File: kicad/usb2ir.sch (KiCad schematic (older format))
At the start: 41 parts, among them J1 USB_A, J2 Conn_01x04_Male, Q1 S8050, Q2 S8050, SW1 SW_Push, U1 YK003, U2 CH340G, U3 LM1117-3.3, U4 STM32F103RBTx, Y1 12M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

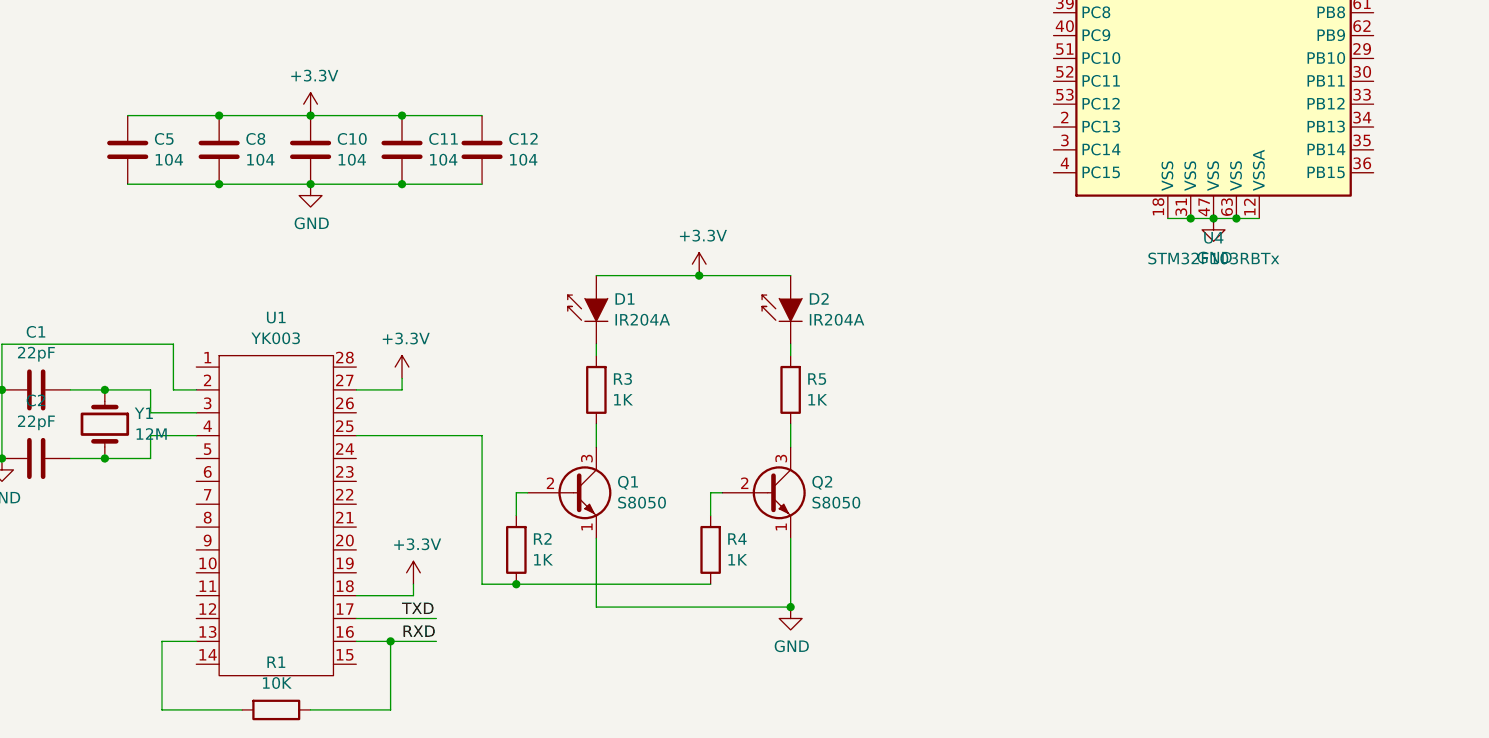
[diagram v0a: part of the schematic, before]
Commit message: 硬件添加红外复制功能
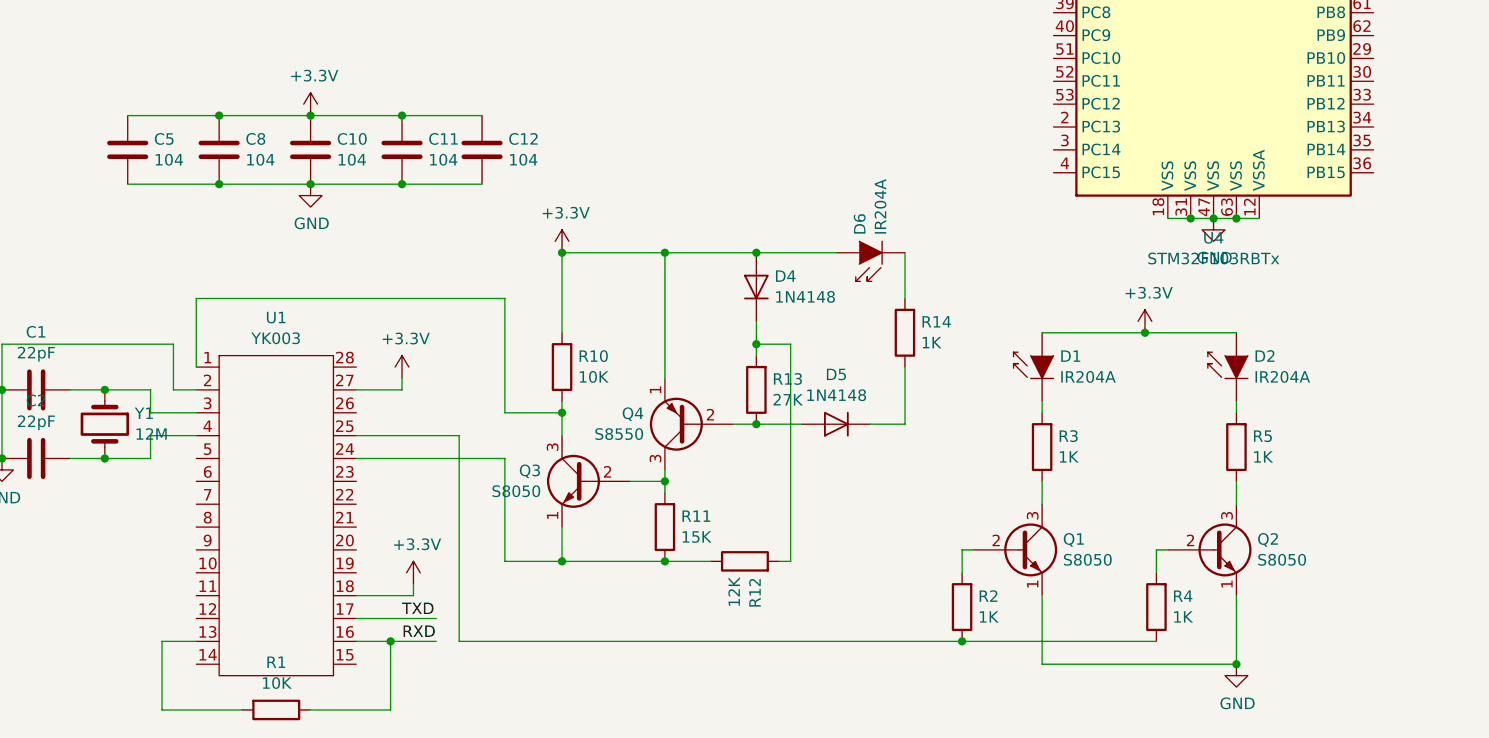
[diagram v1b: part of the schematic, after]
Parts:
- added D4, D5: 1N4148, Diode_SMD:D_0603_1608Metric_Castellated, symbol Diode:1N4148
- added D6: IR204A, LED_THT:LED_D3.0mm_IRBlack, symbol LED:IR204A
- added Q3: S8050, Package_TO_SOT_SMD:SOT-23, symbol Transistor_BJT:S8050
- added Q4: S8550, Package_TO_SOT_SMD:SOT-23, symbol Transistor_BJT:S8550
- added R10: 10K, Resistor_SMD:R_0603_1608Metric_Pad1.05x0.95mm_HandSolder, symbol Device:R
- added R11: 15K, Resistor_SMD:R_0603_1608Metric_Pad1.05x0.95mm_HandSolder, symbol Device:R
- added R12: 12K, Resistor_SMD:R_0603_1608Metric_Pad1.05x0.95mm_HandSolder, symbol Device:R
- added R13: 27K, Resistor_SMD:R_0603_1608Metric_Pad1.05x0.95mm_HandSolder, symbol Device:R
- added R14: 1K, Resistor_SMD:R_0603_1608Metric_Pad1.05x0.95mm_HandSolder, symbol Device:R
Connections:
- wire segments 132 -> 162
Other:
- moved on the sheet: D1, D2, Q1, Q2, R2, R3, R4, R5

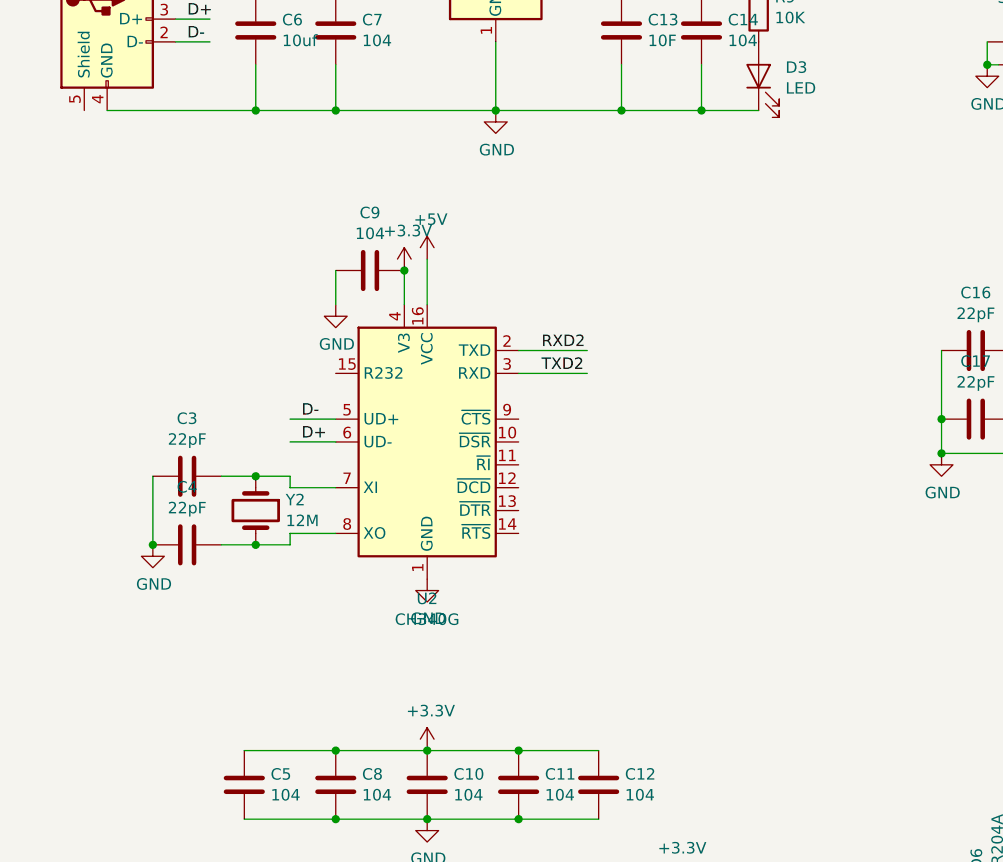
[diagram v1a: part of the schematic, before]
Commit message: 经过长时间的运行发现CH340G偶尔会出现数据丢失情况故现改用cp2104增加稳定性
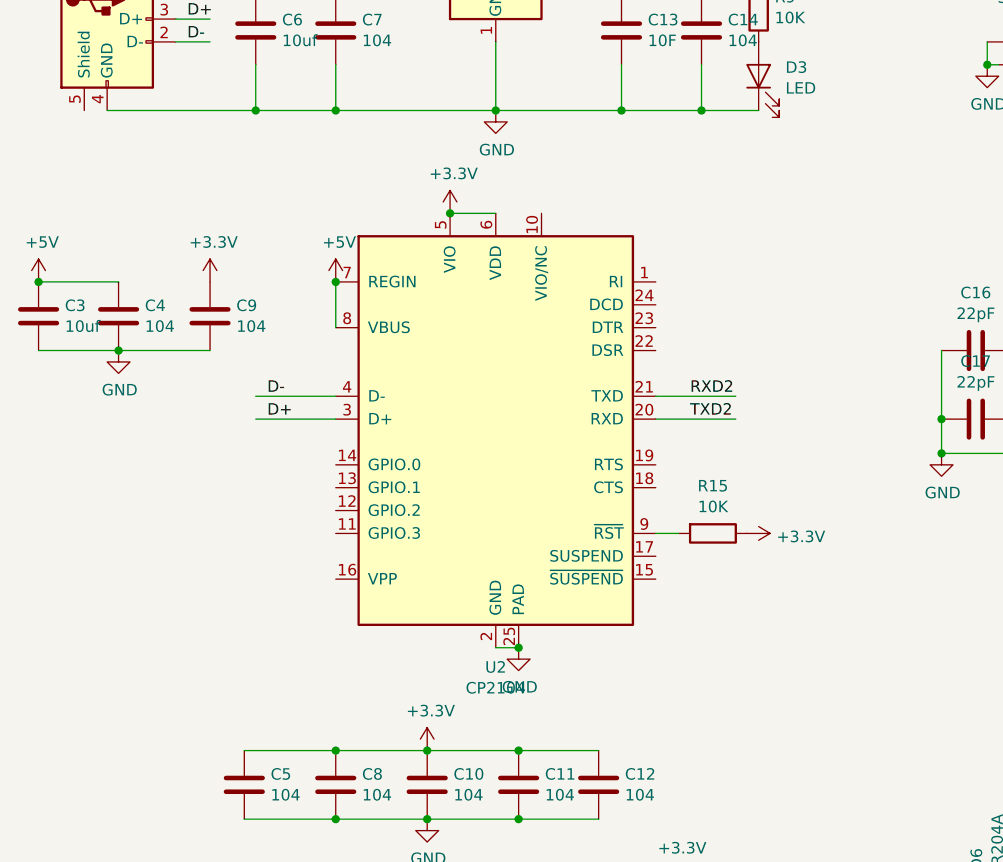
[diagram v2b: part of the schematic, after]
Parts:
- removed U2: CH340G, Package_SO:SOIC-16_3.9x9.9mm_P1.27mm, symbol Interface_USB:CH340G
- removed Y2: 12M, Crystal:Crystal_SMD_5032-2Pin_5.0x3.2mm, symbol Device:Crystal
- added R15: 10K, Resistor_SMD:R_0603_1608Metric_Pad1.05x0.95mm_HandSolder, symbol Device:R
- added U2: CP2104, Package_DFN_QFN:QFN-24-1EP_4x4mm_P0.5mm_EP2.6x2.6mm, symbol Interface_USB:CP2104
- C3: value 22pF -> 10uf
- C4: value 22pF -> 104
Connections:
- wire segments 162 -> 157
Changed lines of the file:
@@
-	1    0    0    -1
-$EndComp
-$Comp
-L Interface_USB:CH340G U2
-U 1 1 6507D2A5
-P 2550 3200
-F 0 "U2" H 2550 2514 50  0000 C CNN
-F 1 "CH340G" H 2550 2423 50  0000 C CNN
-F 2 "Package_SO:SOIC-16_3.9x9.9mm_P1.27mm" H 2600 2650 50  0001 L CNN
-F 3 "http://www.datasheet5.com/pdf-local-2195953" H 2200 4000 50  0001 C CNN
-	1    2550 3200
 	1    0    0    -1
 $EndComp
@@
 Text Label 1500 1450 0    50   ~ 0
 D-
-Text Label 2000 3200 0    50   ~ 0
-D+
-Text Label 2000 3100 0    50   ~ 0
-D-
-Wire Wire Line
-	2150 3100 1950 3100
-Wire Wire Line
-	2150 3200 1950 3200
-$Comp
-L Device:Crystal Y2
-U 1 1 6507DC27
-P 1800 3500
-F 0 "Y2" V 1754 3631 50  0000 L CNN
-F 1 "12M" V 1845 3631 50  0000 L CNN
-F 2 "Crystal:Crystal_SMD_5032-2Pin_5.0x3.2mm" H 1800 3500 50  0001 C CNN
-F 3 "~" H 1800 3500 50  0001 C CNN
-	1    1800 3500
-	0    1    1    0
-$EndComp
-Wire Wire Line
-	1800 3350 1950 3350
-Wire Wire Line
-	1950 3350 1950 3400
-Wire Wire Line
-	1950 3400 2150 3400
-Wire Wire Line
-	1800 3650 1950 3650
-Wire Wire Line
-	1950 3650 1950 3600
-Wire Wire Line
-	1950 3600 2150 3600
-$Comp
-L Device:C C4
-U 1 1 6507E9BB
-P 1500 3650
-F 0 "C4" V 1248 3650 50  0000 C CNN
-F 1 "22pF" V 1339 3650 50  0000 C CNN
-F 2 "Capacitor_SMD:C_0603_1608Metric" H 1538 3500 50  0001 C CNN
-F 3 "~" H 1500 3650 50  0001 C CNN
-	1    1500 3650
-	0    1    1    0
-$EndComp
-$Comp
-L Device:C C3
-U 1 1 6507F0B7
-P 1500 3350
-F 0 "C3" V 1248 3350 50  0000 C CNN
-F 1 "22pF" V 1339 3350 50  0000 C CNN
-F 2 "Capacitor_SMD:C_0603_1608Metric" H 1538 3200 50  0001 C CNN
-F 3 "~" H 1500 3350 50  0001 C CNN
-	1    1500 3350
-	0    1    1    0
-$EndComp
-Wire Wire Line
-	1650 3350 1800 3350
-Connection ~ 1800 3350
-Wire Wire Line
-	1800 3650 1650 3650
-Connection ~ 1800 3650
-Wire Wire Line
-	1350 3650 1350 3350
-$Comp
-L power:GND #PWR02
-U 1 1 6507FC4A
-P 1350 3650
-F 0 "#PWR02" H 1350 3400 50  0001 C CNN
-F 1 "GND" H 1355 3477 50  0000 C CNN
-F 2 "" H 1350 3650 50  0001 C CNN
-F 3 "" H 1350 3650 50  0001 C CNN
-	1    1350 3650
-	1    0    0    -1
-$EndComp
-Connection ~ 1350 3650
-Wire Wire Line
-	2950 2800 3250 2800
-Wire Wire Line
-	2950 2900 3250 2900
-Text Label 3050 2800 0    50   ~ 0
-RXD2
-Text Label 3050 2900 0    50   ~ 0
-TXD2
-Wire Wire Line
-	2550 2400 2550 2600
-$Comp
-L power:GND #PWR07
-U 1 1 6508135F
-P 2550 3800
-F 0 "#PWR07" H 2550 3550 50  0001 C CNN
-F 1 "GND" H 2555 3627 50  0000 C CNN
-F 2 "" H 2550 3800 50  0001 C CNN
-F 3 "" H 2550 3800 50  0001 C CNN
-	1    2550 3800
-	1    0    0    -1
-$EndComp
-$Comp
-L power:GND #PWR04
-U 1 1 6508139E
-P 2150 2600
-F 0 "#PWR04" H 2150 2350 50  0001 C CNN
-F 1 "GND" H 2155 2427 50  0000 C CNN
-F 2 "" H 2150 2600 50  0001 C CNN
-F 3 "" H 2150 2600 50  0001 C CNN
-	1    2150 2600
-	1    0    0    -1
-$EndComp
-$Comp
-L Device:C C9
-U 1 1 650813F5
-P 2300 2450
-F 0 "C9" V 2048 2450 50  0000 C CNN
-F 1 "104" V 2139 2450 50  0000 C CNN
-F 2 "Capacitor_SMD:C_0603_1608Metric" H 2338 2300 50  0001 C CNN
-F 3 "~" H 2300 2450 50  0001 C CNN
-	1    2300 2450
-	0    1    1    0
-$EndComp
-Wire Wire Line
-	2150 2600 2150 2450
-Wire Wire Line
-	2450 2600 2450 2450
-$Comp
-L power:+5V #PWR06
-U 1 1 65081DD3
-P 2550 2400
-F 0 "#PWR06" H 2550 2250 50  0001 C CNN
-F 1 "+5V" H 2565 2573 50  0000 C CNN
-F 2 "" H 2550 2400 50  0001 C CNN
-F 3 "" H 2550 2400 50  0001 C CNN
-	1    2550 2400
-	1    0    0    -1
-$EndComp
-$Comp
-L power:+3.3V #PWR05
-U 1 1 65081E14
-P 2450 2450
-F 0 "#PWR05" H 2450 2300 50  0001 C CNN
-F 1 "+3.3V" H 2465 2623 50  0000 C CNN
-F 2 "" H 2450 2450 50  0001 C CNN
-F 3 "" H 2450 2450 50  0001 C CNN
-	1    2450 2450
-	1    0    0    -1
-$EndComp
-Connection ~ 2450 2450
 $Comp
 L Device:C C5
@@
 Wire Wire Line
 	3200 6850 5400 6850
+$Comp
+L Interface_USB:CP2104 U2
+U 1 1 650941A6
+P 2850 3100
+F 0 "U2" H 2850 2014 50  0000 C CNN
+F 1 "CP2104" H 2850 1923 50  0000 C CNN
+F 2 "Package_DFN_QFN:QFN-24-1EP_4x4mm_P0.5mm_EP2.6x2.6mm" H 3000 2150 50  0001 L CNN
+F 3 "https://www.silabs.com/Support%20Documents/TechnicalDocs/cp2104.pdf" H 2300 4350 50  0001 C CNN
+	1    2850 3100
+	1    0    0    -1
+$EndComp
+Wire Wire Line
+	2150 3000 1800 3000
+Wire Wire Line
+	2150 3100 1800 3100
+Text Label 1850 3000 0    50   ~ 0
+D-
+Text Label 1850 3100 0    50   ~ 0
+D+
+Wire Wire Line
+	3550 3000 3900 3000
+Wire Wire Line
+	3550 3100 3900 3100
+Text Label 3700 3000 0    50   ~ 0
+RXD2
+Text Label 3700 3100 0    50   ~ 0
+TXD2
+$Comp
+L power:GND #PWR0103
+U 1 1 650C60A7
+P 2950 4100
+F 0 "#PWR0103" H 2950 3850 50  0001 C CNN
+F 1 "GND" H 2955 3927 50  0000 C CNN
+F 2 "" H 2950 4100 50  0001 C CNN
+F 3 "" H 2950 4100 50  0001 C CNN
+	1    2950 4100
+	1    0    0    -1
+$EndComp
+Wire Wire Line
+	2850 4100 2950 4100
+Connection ~ 2950 4100
+Wire Wire Line
+	2650 2200 2850 2200
+$Comp
+L power:+3.3V #PWR0104
+U 1 1 650D76F9
+P 2650 2200
+F 0 "#PWR0104" H 2650 2050 50  0001 C CNN
+F 1 "+3.3V" H 2665 2373 50  0000 C CNN
+F 2 "" H 2650 2200 50  0001 C CNN
+F 3 "" H 2650 2200 50  0001 C CNN
+	1    2650 2200
+	1    0    0    -1
+$EndComp
+Connection ~ 2650 2200
+Wire Wire Line
+	2150 2700 2150 2500
+$Comp
+L power:+5V #PWR0105
+U 1 1 650E0341
+P 2150 2500
+F 0 "#PWR0105" H 2150 2350 50  0001 C CNN
+F 1 "+5V" H 2165 2673 50  0000 C CNN
+F 2 "" H 2150 2500 50  0001 C CNN
+F 3 "" H 2150 2500 50  0001 C CNN
+	1    2150 2500
+	1    0    0    -1
+$EndComp
+Connection ~ 2150 2500
+$Comp
+L Device:R R15
+U 1 1 650E0732
+P 3800 3600
+F 0 "R15" V 3593 3600 50  0000 C CNN
+F 1 "10K" V 3684 3600 50  0000 C CNN
+F 2 "Resistor_SMD:R_0603_1608Metric_Pad1.05x0.95mm_HandSolder" V 3730 3600 50  0001 C CNN
+F 3 "~" H 3800 3600 50  0001 C CNN
+	1    3800 3600
+	0    1    1    0
+$EndComp
+Wire Wire Line
+	3650 3600 3550 3600
+$Comp
+L power:+3.3V #PWR0106
+U 1 1 650E95C5
+P 3950 3600
+F 0 "#PWR0106" H 3950 3450 50  0001 C CNN
+F 1 "+3.3V" V 3965 3728 50  0000 L CNN
+F 2 "" H 3950 3600 50  0001 C CNN
+F 3 "" H 3950 3600 50  0001 C CNN
+	1    3950 3600
+	0    1    1    0
+$EndComp
+$Comp
+L Device:C C3
+U 1 1 650F280E
+P 850 2650
+F 0 "C3" H 965 2696 50  0000 L CNN
+F 1 "10uf" H 965 2605 50  0000 L CNN
+F 2 "Capacitor_SMD:C_0603_1608Metric" H 888 2500 50  0001 C CNN
+F 3 "~" H 850 2650 50  0001 C CNN
+	1    850  2650
+	1    0    0    -1
+$EndComp
+$Comp
+L Device:C C4
+U 1 1 650F28F2
+P 1200 2650
+F 0 "C4" H 1315 2696 50  0000 L CNN
+F 1 "104" H 1315 2605 50  0000 L CNN
+F 2 "Capacitor_SMD:C_0603_1608Metric" H 1238 2500 50  0001 C CNN
+F 3 "~" H 1200 2650 50  0001 C CNN
+	1    1200 2650
+	1    0    0    -1
+$EndComp
+$Comp
+L Device:C C9
+U 1 1 650F2A49
+P 1600 2650
+F 0 "C9" H 1715 2696 50  0000 L CNN
+F 1 "104" H 1715 2605 50  0000 L CNN
+F 2 "Capacitor_SMD:C_0603_1608Metric" H 1638 2500 50  0001 C CNN
+F 3 "~" H 1600 2650 50  0001 C CNN
+	1    1600 2650
+	1    0    0    -1
+$EndComp
+Wire Wire Line
+	850  2500 1200 2500
+Wire Wire Line
+	850  2800 1200 2800
+Connection ~ 1200 2800
+Wire Wire Line
+	1200 2800 1600 2800
+$Comp
+L power:GND #PWR0107
+U 1 1 65104E45
+P 1200 2800
+F 0 "#PWR0107" H 1200 2550 50  0001 C CNN
+F 1 "GND" H 1205 2627 50  0000 C CNN
+F 2 "" H 1200 2800 50  0001 C CNN
+F 3 "" H 1200 2800 50  0001 C CNN
+	1    1200 2800
+	1    0    0    -1
+$EndComp
+$Comp
+L power:+5V #PWR0108
+U 1 1 65104EE5
+P 850 2500
+F 0 "#PWR0108" H 850 2350 50  0001 C CNN
+F 1 "+5V" H 865 2673 50  0000 C CNN
+F 2 "" H 850 2500 50  0001 C CNN
+F 3 "" H 850 2500 50  0001 C CNN
+	1    850  2500
+	1    0    0    -1
+$EndComp
+$Comp
+L power:+3.3V #PWR0109
+U 1 1 65104F93
+P 1600 2500
+F 0 "#PWR0109" H 1600 2350 50  0001 C CNN
+F 1 "+3.3V" H 1615 2673 50  0000 C CNN
+F 2 "" H 1600 2500 50  0001 C CNN
+F 3 "" H 1600 2500 50  0001 C CNN
+	1    1600 2500
+	1    0    0    -1
+$EndComp
+Connection ~ 850  2500
 $EndSCHEMATC
